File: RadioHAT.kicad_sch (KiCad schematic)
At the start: 36 parts, among them J1 RPi_GPIO, J3 Conn_02x07_Odd_Even, J4 Conn_02x07_Odd_Even, U1 INA219AxD, U2 LP3855-ADJ

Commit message: Add 5V power channel for PCI cards
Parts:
- added JP3: SolderJumper_2_Bridged, Jumper:SolderJumper-2_P1.3mm_Bridged_Pad1.0x1.5mm, symbol Jumper:SolderJumper_2_Bridged
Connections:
- net +5V: now also JP3.2 (B)
- net at J2.28 (5V): now also J2.48 (5V), J2.6 (5V), JP3.1 (A)
- no-connect marks 11 -> 8
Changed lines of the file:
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@@
 	)
 	(junction
+		(at 252.73 36.83)
+		(diameter 0)
+		(color 0 0 0 0)
+	)
+	(junction
 		(at 240.03 95.25)
 		(diameter 0)
@@
 	)
 	(junction
+		(at 255.27 36.83)
+		(diameter 0)
+		(color 0 0 0 0)
+	)
+	(junction
 		(at 222.25 83.82)
 		(diameter 0)
@@
 	)
 	(no_connect
-		(at 250.19 39.37)
-	)
-	(no_connect
 		(at 267.97 53.34)
 	)
@@
 		(at 267.97 55.88)
 	)
-	(no_connect
-		(at 255.27 39.37)
-	)
-	(no_connect
-		(at 252.73 39.37)
-	)
 	(wire
 		(pts
@@
 	(wire
 		(pts
+			(xy 255.27 22.86) (xy 255.27 25.4)
+		)
+		(stroke
+			(width 0)
+			(type default)
+		)
+	)
+	(wire
+		(pts
 			(xy 217.17 58.42) (xy 224.79 58.42)
 		)
@@
 	(wire
 		(pts
+			(xy 255.27 33.02) (xy 255.27 36.83)
+		)
+		(stroke
+			(width 0)
+			(type default)
+		)
+	)
+	(wire
+		(pts
 			(xy 184.15 106.68) (xy 184.15 104.14)
 		)
@@
 	(wire
 		(pts
+			(xy 252.73 36.83) (xy 250.19 36.83)
+		)
+		(stroke
+			(width 0)
+			(type default)
+		)
+	)
+	(wire
+		(pts
 			(xy 176.53 93.98) (xy 179.07 93.98)
 		)
@@
 	(wire
 		(pts
+			(xy 255.27 36.83) (xy 255.27 39.37)
+		)
+		(stroke
+			(width 0)
+			(type default)
+		)
+	)
+	(wire
+		(pts
 			(xy 137.16 86.36) (xy 142.24 86.36)
 		)
@@
 	(wire
 		(pts
+			(xy 252.73 36.83) (xy 252.73 39.37)
+		)
+		(stroke
+			(width 0)
+			(type default)
+		)
+	)
+	(wire
+		(pts
 			(xy 166.37 78.74) (xy 168.91 78.74)
 		)
@@
 	(wire
 		(pts
+			(xy 255.27 36.83) (xy 252.73 36.83)
+		)
+		(stroke
+			(width 0)
+			(type default)
+		)
+	)
+	(wire
+		(pts
 			(xy 246.38 95.25) (xy 246.38 97.79)
 		)
@@
 	(wire
 		(pts
+			(xy 250.19 39.37) (xy 250.19 36.83)
+		)
+		(stroke
+			(width 0)
+			(type default)
+		)
+	)
+	(wire
+		(pts
 			(xy 234.95 93.98) (xy 234.95 95.25)
 		)
@@
 	)
 	(symbol
+		(lib_id "power:+5V")
+		(at 255.27 22.86 0)
+		(unit 1)
+		(exclude_from_sim no)
+		(in_bom yes)
+		(on_board yes)
+		(dnp no)
+		(fields_autoplaced yes)
+		(property "Reference" "#PWR021"
+			(at 255.27 26.67 0)
+			(effects
+				(font
+					(size 1.27 1.27)
+				)
+				(hide yes)
+			)
+		)
+		(property "Value" "+5V"
+			(at 255.27 17.78 0)
+			(effects
+				(font
+					(size 1.27 1.27)
+				)
+			)
+		)
+		(property "Footprint" ""
+			(at 255.27 22.86 0)
+			(effects
+				(font
+					(size 1.27 1.27)
+				)
+				(hide yes)
+			)
+		)
+		(property "Datasheet" ""
+			(at 255.27 22.86 0)
+			(effects
+				(font
+					(size 1.27 1.27)
+				)
+				(hide yes)
+			)
+		)
+		(property "Description" "Power symbol creates a global label with name \"+5V\""
+			(at 255.27 22.86 0)
+			(effects
+				(font
+					(size 1.27 1.27)
+				)
+				(hide yes)
+			)
+		)
+		(pin "1"
+		)
+		(instances
+			(project "RadioHAT"
+				(path "/b81b30b5-0f95-4689-93f2-268be91e8e59"
+					(reference "#PWR021")
+					(unit 1)
+				)
+			)
+		)
+	)
+	(symbol
 		(lib_id "power:GND")
 		(at 41.91 90.17 0)
@@
 					(unit 1)
 				)
+			)
+		)
+	)
+	(symbol
+		(lib_id "Jumper:SolderJumper_2_Bridged")
+		(at 255.27 29.21 90)
+		(unit 1)
+		(exclude_from_sim no)
+		(in_bom no)
+		(on_board yes)
+		(dnp no)
+		(fields_autoplaced yes)
+		(property "Reference" "JP3"
+			(at 257.81 27.9399 90)
+			(effects
+				(font
+					(size 1.27 1.27)
+				)
+				(justify right)
+			)
+		)
+		(property "Value" "SolderJumper_2_Bridged"
+			(at 257.81 30.4799 90)
+			(effects
+				(font
+					(size 1.27 1.27)
+				)
+				(justify right)
+			)
+		)
+		(property "Footprint" "Jumper:SolderJumper-2_P1.3mm_Bridged_Pad1.0x1.5mm"
+			(at 255.27 29.21 0)
+			(effects
+				(font
+					(size 1.27 1.27)
+				)
+				(hide yes)
+			)
+		)
+		(property "Datasheet" "~"
+			(at 255.27 29.21 0)
+			(effects
+				(font
+					(size 1.27 1.27)
+				)
+				(hide yes)
+			)
+		)
+		(property "Description" "Solder Jumper, 2-pole, closed/bridged"
+			(at 255.27 29.21 0)
+			(effects
+				(font
+					(size 1.27 1.27)
+				)
+				(hide yes)
+			)
+		)
+		(pin "2"
+		)
+		(pin "1"
+		)
+		(instances
+			(project ""
+				(path "/b81b30b5-0f95-4689-93f2-268be91e8e59"
+					(reference "JP3")
+					(unit 1)
+				)

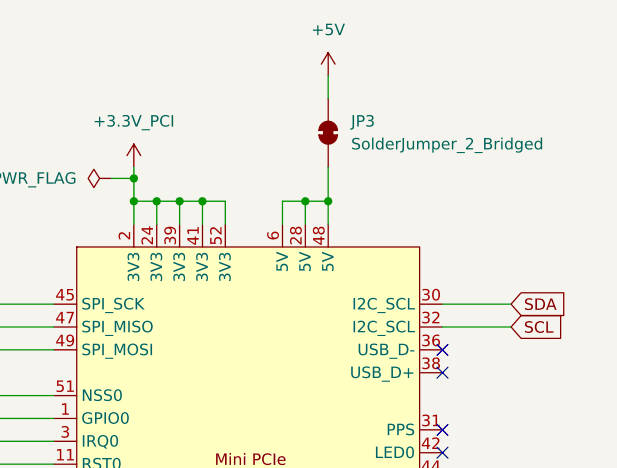
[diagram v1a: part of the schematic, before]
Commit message: Fix missing power flag
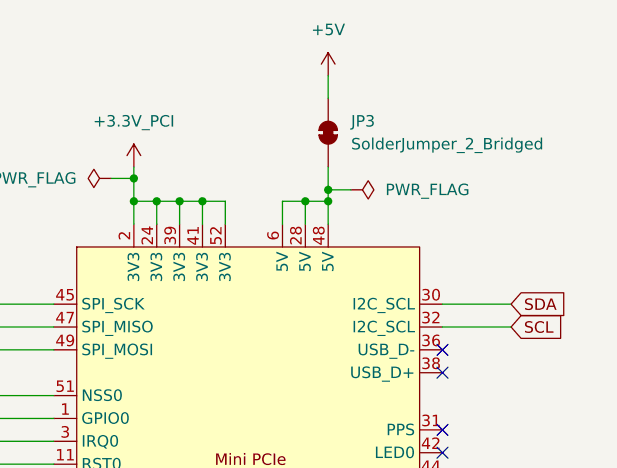
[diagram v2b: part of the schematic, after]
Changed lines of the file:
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@@
 	)
 	(junction
+		(at 255.27 35.56)
+		(diameter 0)
+		(color 0 0 0 0)
+	)
+	(junction
 		(at 234.95 95.25)
 		(diameter 0)
@@
 	(wire
 		(pts
+			(xy 255.27 35.56) (xy 257.81 35.56)
+		)
+		(stroke
+			(width 0)
+			(type default)
+		)
+	)
+	(wire
+		(pts
 			(xy 163.83 88.9) (xy 163.83 93.98)
 		)
@@
 	(wire
 		(pts
-			(xy 255.27 33.02) (xy 255.27 36.83)
+			(xy 255.27 33.02) (xy 255.27 35.56)
 		)
 		(stroke
@@
 	(wire
 		(pts
+			(xy 255.27 35.56) (xy 255.27 36.83)
+		)
+		(stroke
+			(width 0)
+			(type default)
+		)
+	)
+	(wire
+		(pts
 			(xy 31.75 62.23) (xy 44.45 62.23)
 		)
@@
 					(unit 1)
 				)
+			)
+		)
+	)
+	(symbol
+		(lib_id "power:PWR_FLAG")
+		(at 257.81 35.56 270)
+		(unit 1)
+		(exclude_from_sim no)
+		(in_bom yes)
+		(on_board yes)
+		(dnp no)
+		(property "Reference" "#FLG05"
+			(at 259.715 35.56 0)
+			(effects
+				(font
+					(size 1.27 1.27)
+				)
+				(hide yes)
+			)
+		)
+		(property "Value" "PWR_FLAG"
+			(at 261.62 35.5599 90)
+			(effects
+				(font
+					(size 1.27 1.27)
+				)
+				(justify left)
+			)
+		)
+		(property "Footprint" ""
+			(at 257.81 35.56 0)
+			(effects
+				(font
+					(size 1.27 1.27)
+				)
+				(hide yes)
+			)
+		)
+		(property "Datasheet" "~"
+			(at 257.81 35.56 0)
+			(effects
+				(font
+					(size 1.27 1.27)
+				)
+				(hide yes)
+			)
+		)
+		(property "Description" "Special symbol for telling ERC where power comes from"
+			(at 257.81 35.56 0)
+			(effects
+				(font
+					(size 1.27 1.27)
+				)
+				(hide yes)
+			)
+		)
+		(pin "1"
+		)
+		(instances
+			(project "RadioHAT"
+				(path "/b81b30b5-0f95-4689-93f2-268be91e8e59"
+					(reference "#FLG05")
+					(unit 1)
+				)

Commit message: Add part numbers
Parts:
- J3, J4: Mouser (none) -> 523-G800LW589018EU
- R1, R10, R11, R12, R13, R2, R3, R4, R5, R6, R7, R8, R9: Mouser (none) -> 603-AC0603JR-131KL
